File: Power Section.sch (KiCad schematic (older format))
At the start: 64 parts, among them IC1 CYPD3177, J17 CK-JS102011SAQN, J4 USB_C_Receptacle_USB2.0, Q1 IRLML9301TRPBF, Q2 IRLML9301TRPBF, Q3 IRLML9301TRPBF, Q7 IRLML9301TRPBF, U1 LM1117LDX, U2 LDFM33PVR, U5 MCP73213, U6 ETA3000

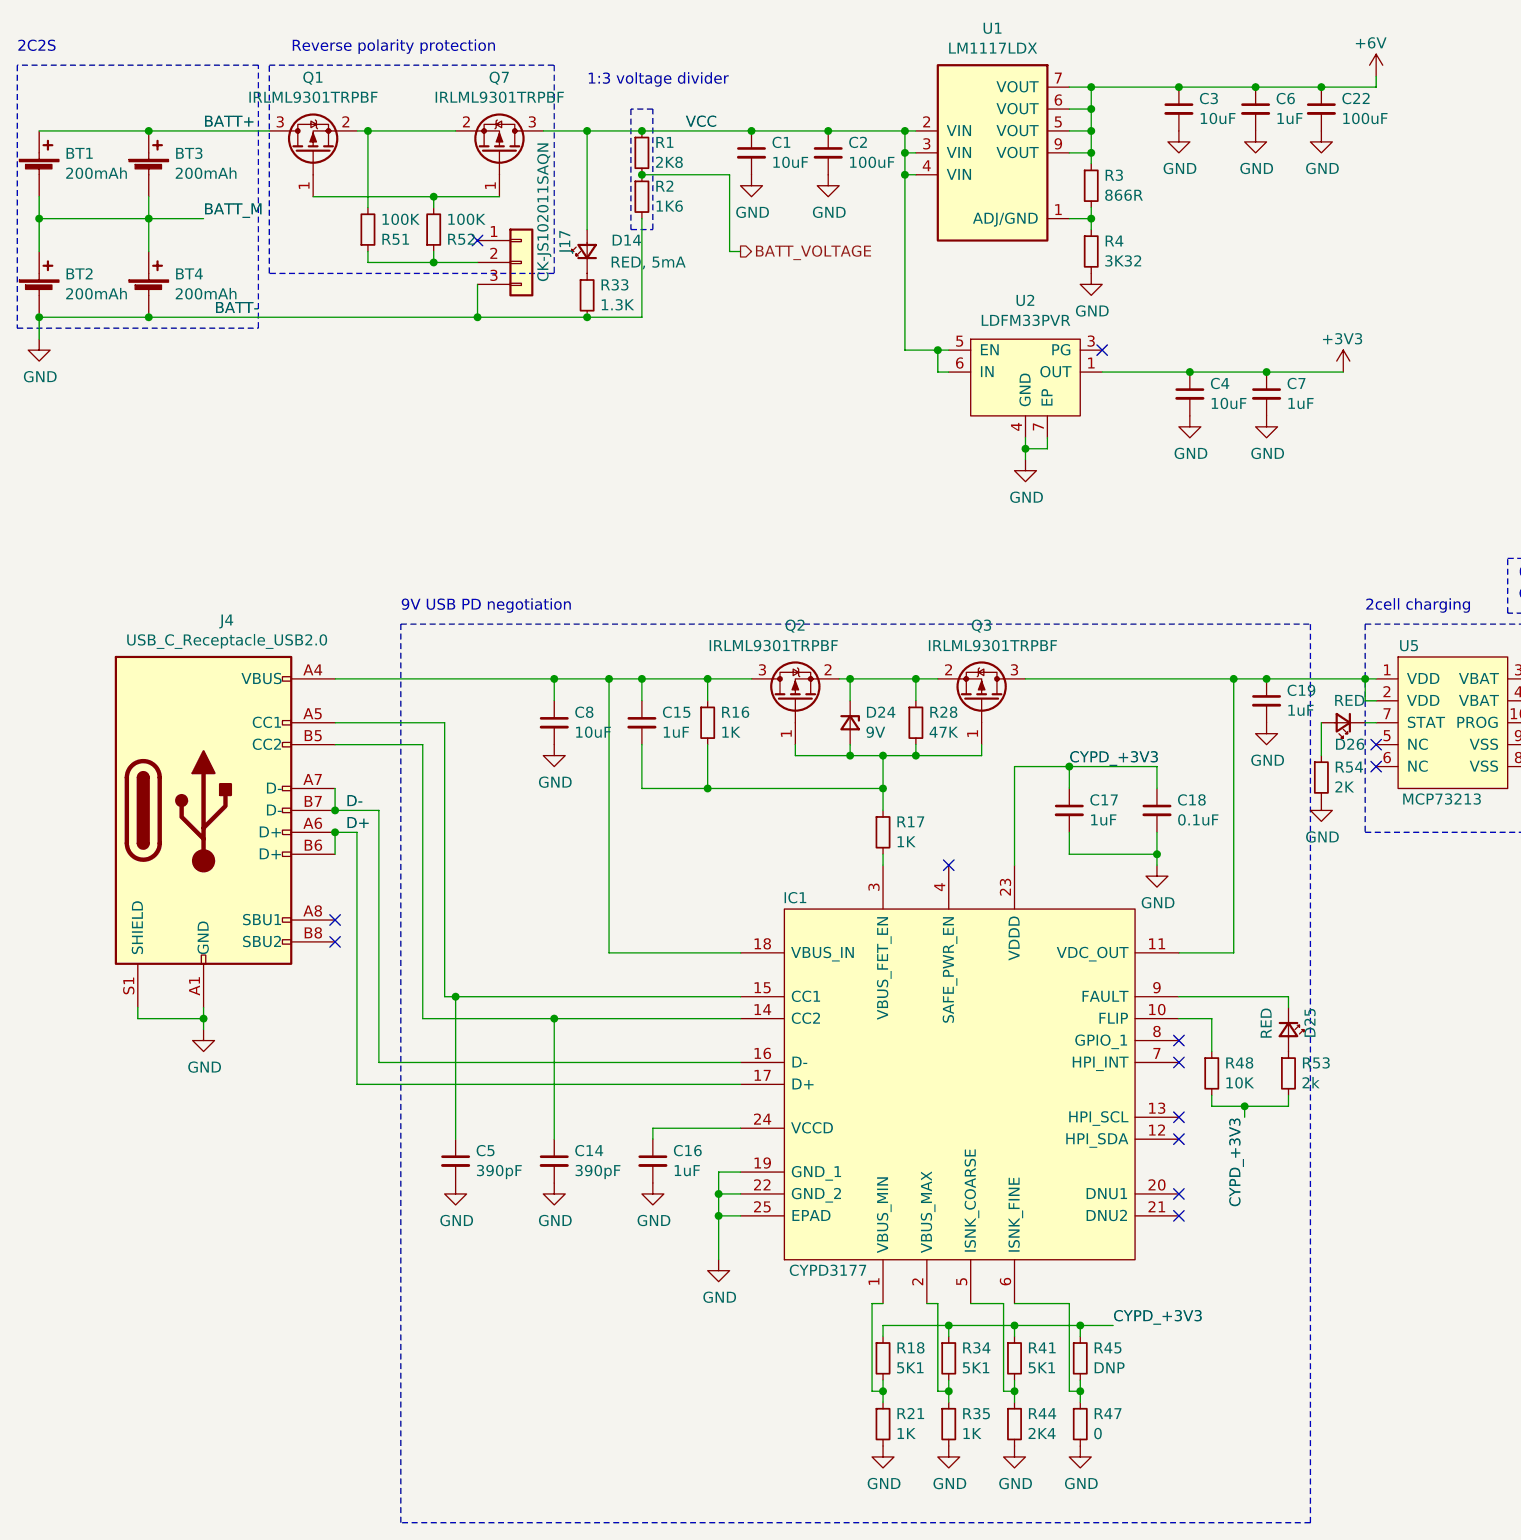
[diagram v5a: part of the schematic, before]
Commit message: Zmieniono kontroler USB-PD
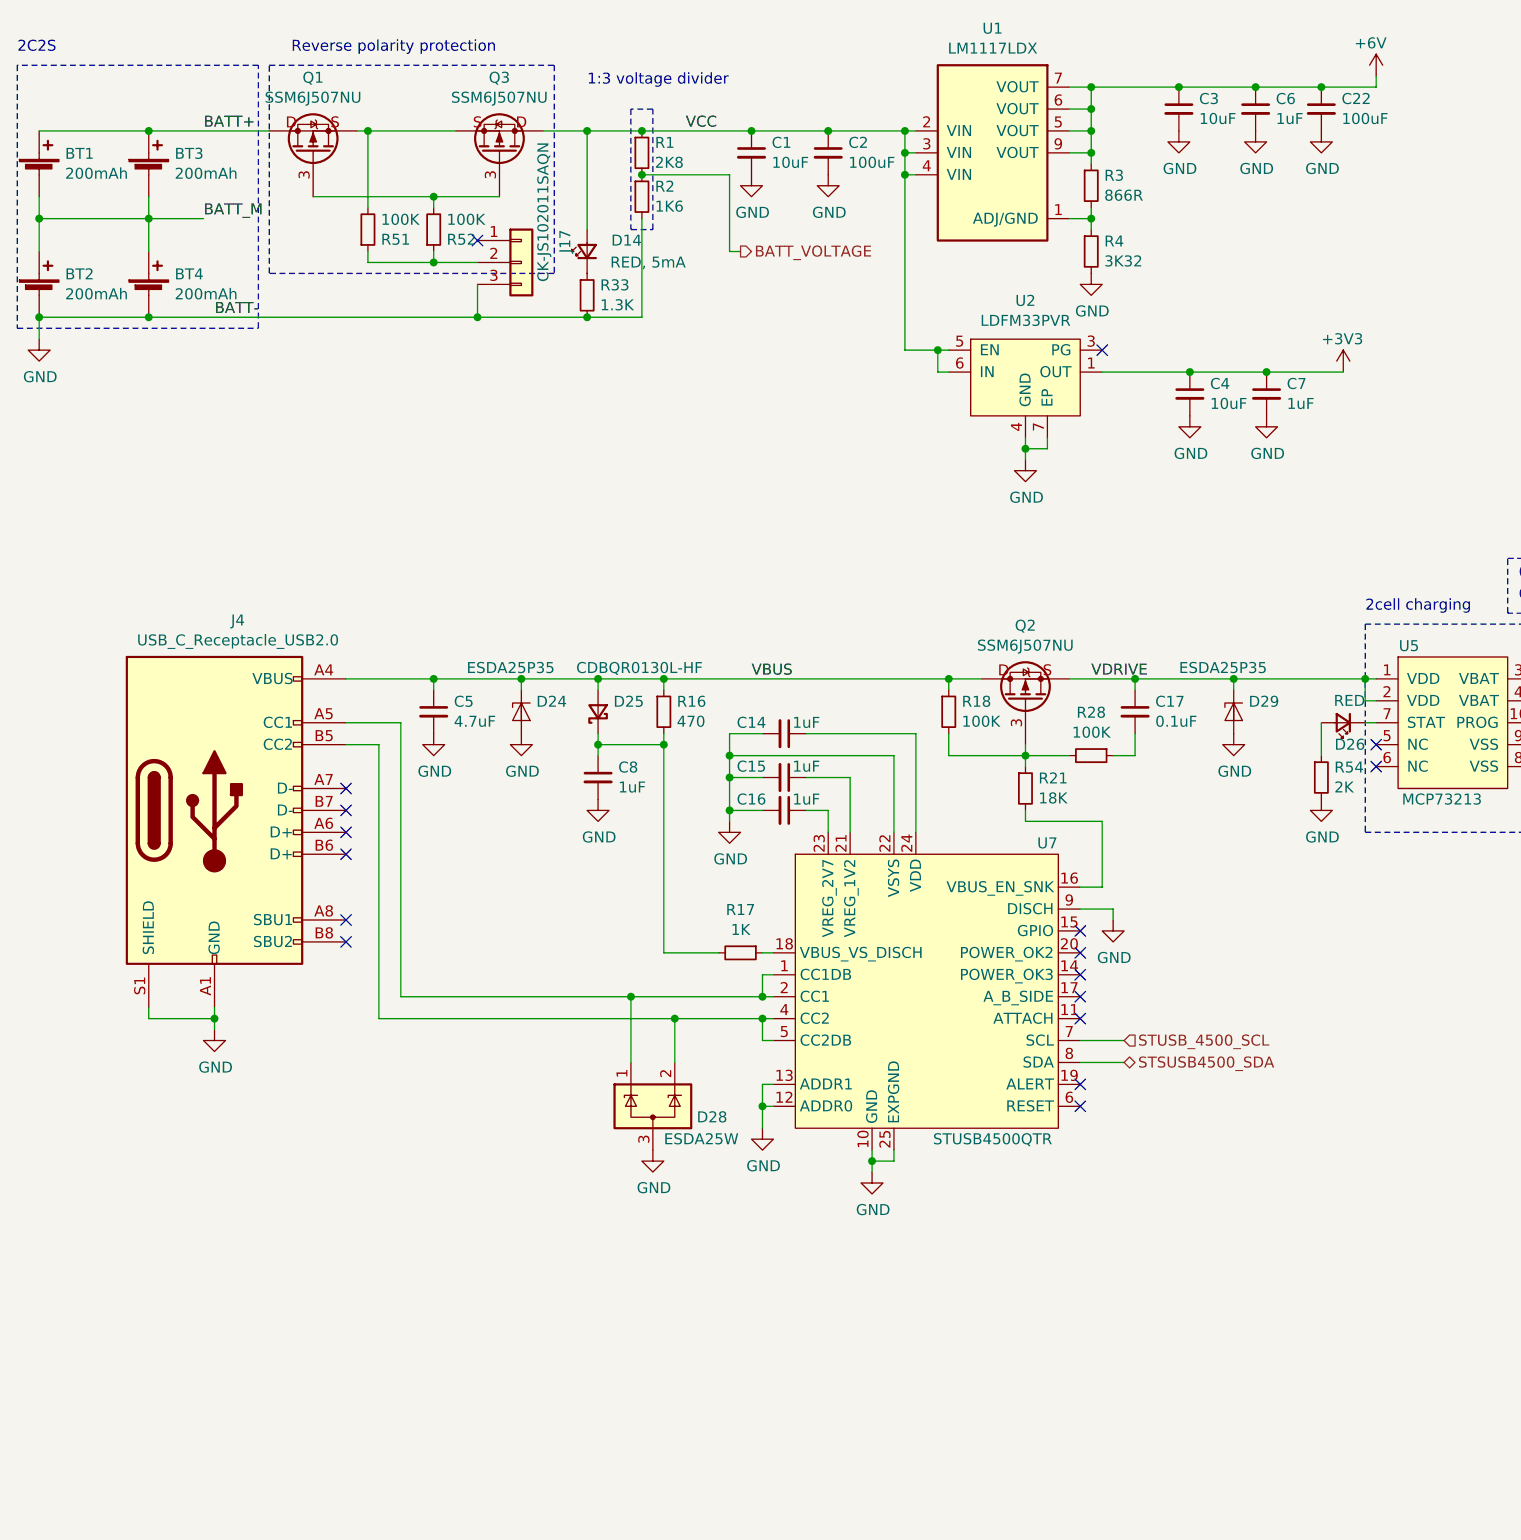
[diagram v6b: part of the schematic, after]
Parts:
- removed C18: 0.1uF, Capacitor_SMD:C_0402_1005Metric, symbol Device:C_Small
- removed C19: 1uF, Capacitor_SMD:C_0402_1005Metric, symbol Device:C_Small
- removed D24: 9V, Diode_SMD:D_SOD-52, symbol Device:D_Zener_Small
- removed D25: RED, LED_SMD:LED_0402_1005Metric, symbol Device:LED_Small
- removed IC1: CYPD3177, CYPD3177-24LQXI:QFN50P400X400X60-25N-D, symbol CYPD3177-24LQXI:CYPD3177
- removed Q1, Q2, Q3, Q7: IRLML9301TRPBF, Package_TO_SOT_SMD:SOT-23, symbol Device:Q_PMOS_GSD
- removed R34, R41: 5K1, Resistor_SMD:R_0402_1005Metric, symbol Device:R_Small
- removed R35: 1K, Resistor_SMD:R_0402_1005Metric, symbol Device:R_Small
- removed R44: 2K4, Resistor_SMD:R_0402_1005Metric, symbol Device:R_Small
- removed R45: DNP, Resistor_SMD:R_0402_1005Metric, symbol Device:R_Small
- removed R47: 0, Resistor_SMD:R_0402_1005Metric, symbol Device:R_Small
- removed R48: 10K, Resistor_SMD:R_0402_1005Metric, symbol Device:R_Small
- removed R53: 2k, Resistor_SMD:R_0402_1005Metric, symbol Device:R_Small
- added D24, D29: ESDA25P35, footprints:1610, symbol synermycha-electronics:ESDA25P35
- added D25: CDBQR0130L-HF, Diode_SMD:D_0402_1005Metric, symbol Device:D_Schottky_Small
- added D28: ESDA25W, Package_TO_SOT_SMD:SOT-323_SC-70, symbol synermycha-electronics:ESDA25W
- added Q1, Q2, Q3: SSM6J507NU, footprints:UDFN6B, symbol synermycha-electronics:SSM6J507NU
- added U7: STUSB4500QTR, Package_DFN_QFN:QFN-24-1EP_4x4mm_P0.5mm_EP2.7x2.7mm, symbol synermycha-electronics:STUSB4500QTR
- C14: value 390pF -> 1uF
- C17: value 1uF -> 0.1uF
- C5: value 390pF -> 4.7uF; footprint Capacitor_SMD:C_0402_1005Metric -> Capacitor_SMD:C_0603_1608Metric
- C8: value 10uF -> 1uF; footprint Capacitor_SMD:C_0603_1608Metric -> Capacitor_SMD:C_0402_1005Metric
- R16: value 1K -> 470
- R18: value 5K1 -> 100K
- R21: value 1K -> 18K
- R28: value 47K -> 100K
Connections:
- net BATT+: now also Q1.1 (D), Q1.2 (D), Q1.5 (D), Q1.6 (D), Q1.D
- net GND: now also C15.2, D24.2 (A), D28.3 (A), D29.2 (A), U7.10 (GND), U7.12 (ADDR0), U7.13 (ADDR1), U7.22 (VSYS), U7.25 (EXPGND), U7.9 (DISCH); no longer C17.2, R21.2
- net VCC: now also Q3.1 (D), Q3.2 (D), Q3.5 (D), Q3.6 (D), Q3.D
- net at R52.2: now also Q1.3 (G), Q3.3 (G)
- net at R51.2: now also Q1.4 (S), Q1.S, Q3.4 (S), Q3.S
- net at R18.2, R21.1: now also R28.2, Q2.3 (G)
- net VDRIVE: now reaches U5.1 (VDD), U5.2 (VDD)
- net VDRIVE: now also C17.1, D29.1 (K1), Q2.4 (S), Q2.S
- net at J4.B5 (CC2): now also D28.2 (K), U7.4 (CC2), U7.5 (CC2DB); no longer C14.1
- net at J4.A5 (CC1): now also D28.1 (K), U7.1 (CC1DB), U7.2 (CC1); no longer C5.1
- net VBUS: now reaches J4.A4 (VBUS), J4.A9 (VBUS), J4.B4 (VBUS), J4.B9 (VBUS), R16.1
- net VBUS: now also C5.1, R18.1, D24.1 (K1), D25.2 (A), Q2.1 (D), Q2.2 (D), Q2.5 (D), Q2.6 (D), Q2.D; no longer C15.1, C8.1
- net at C16.1: now also U7.23 (VREG_2V7)
- net at R17.2: now also C8.1, R16.2, D25.1 (K)
- net at R28.1: now also C17.2
- removed net CYPD_+3V3: C17.1, R18.1
- net D+: no longer names the net of J4.A6 (D+)
- net D+: no longer J4.B6 (D+)
- net D-: no longer names the net of J4.A7 (D-)
- net D-: no longer J4.B7 (D-)
- new net: R21.2, U7.16 (VBUS_EN_SNK)
- new net: R17.1, U7.18 (VBUS_VS_DISCH)
- new net: C15.1, U7.21 (VREG_1V2)
- new net: C14.1, U7.24 (VDD)
- new net STSUSB4500_SDA: U7.8 (SDA)
- new net STUSB_4500_SCL: U7.7 (SCL)
- no-connect marks 14 -> 18
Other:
- note removed: "9V USB PD negotiation"
- moved on the sheet: J4
